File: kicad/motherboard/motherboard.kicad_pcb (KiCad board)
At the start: 4 copper layers, 180.3 x 281.9 mm, 53 parts, among them J1 DB37_Female, J10 DB37_Female, J11 DB37_Female, J12 Barrel_Jack, J13 TSR 1-2433, J2 DB37_Female, J3 DB37_Female, J4 DB37_Female, J5 DB37_Female, J6 DB25_Female, J7 DB37_Female, J8 DB25_Female, J9 DB9_Female, SW1 SW_SPST, U1 SN74ALVC00, U10 SN74ALVC00, U11 SN74ALVC00, U12 SN74ALVC00, U13 SN74ALVC00, U14 SN74ALVC00, U15 SN74ALVC00, U16 SN74ALVC00, U17 SN74ALVC00, U18 SN74ALVC00, U19 SN74ALVC00, U2 SN74ALVC00, U20 SN74ALVC00, U21 SN74ALVC00, U22 SN74ALVC00, U23 SN74ALVC00, U24 SN74ALVC00, U25 SN74ALVC00, U26 SN74ALVC00, U27 SN74ALVC00, U28 SN74ALVC00, U29 SN74ALVC00, U3 SN74ALVC00, U30 SN74ALVC00, U31 SN74ALVC00, U32 SN74ALVC00, U4 SN74ALVC00, U5 SN74ALVC00, U6 SN74ALVC00, U7 SN74ALVC00, U8 SN74ALVC00, U9 SN74ALVC00

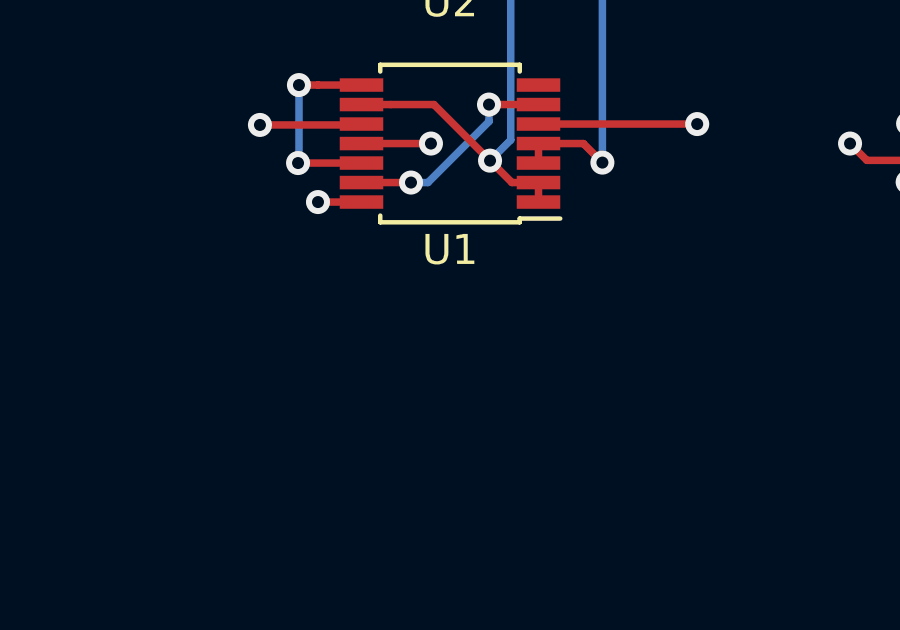
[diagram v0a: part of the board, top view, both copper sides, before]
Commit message: Added clock output enable signal to motherboard debugger. Updated component library.
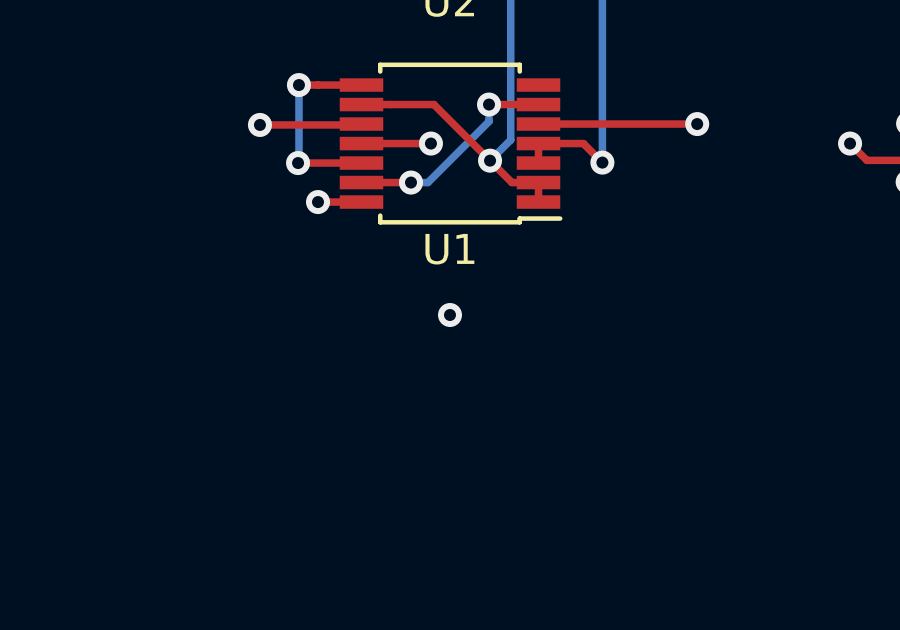
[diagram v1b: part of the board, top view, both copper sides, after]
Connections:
- J11 pad 1: +3V3 -> GND
- J11 pad 20: GND -> clk_oe
- J9 pad 3: Net-(J9-Pad3) -> clk_oe
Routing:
- net clk_oe: track 0.00 -> 297.9 mm, vias 0 -> 1

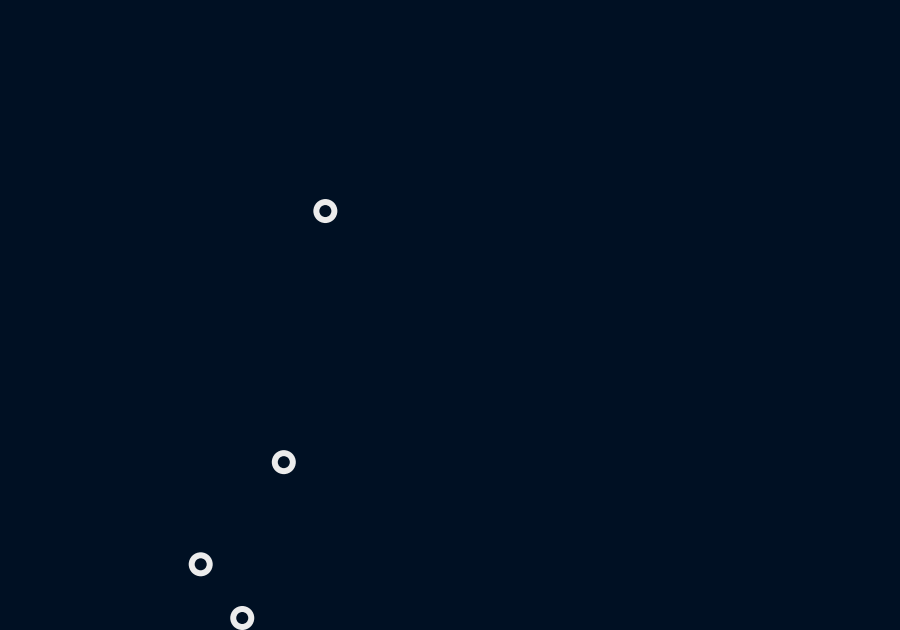
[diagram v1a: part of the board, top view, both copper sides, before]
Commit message: ALU schematic, layout, routing complete. Associated motherboardmod. Also added Load LED to register and program counter boards.
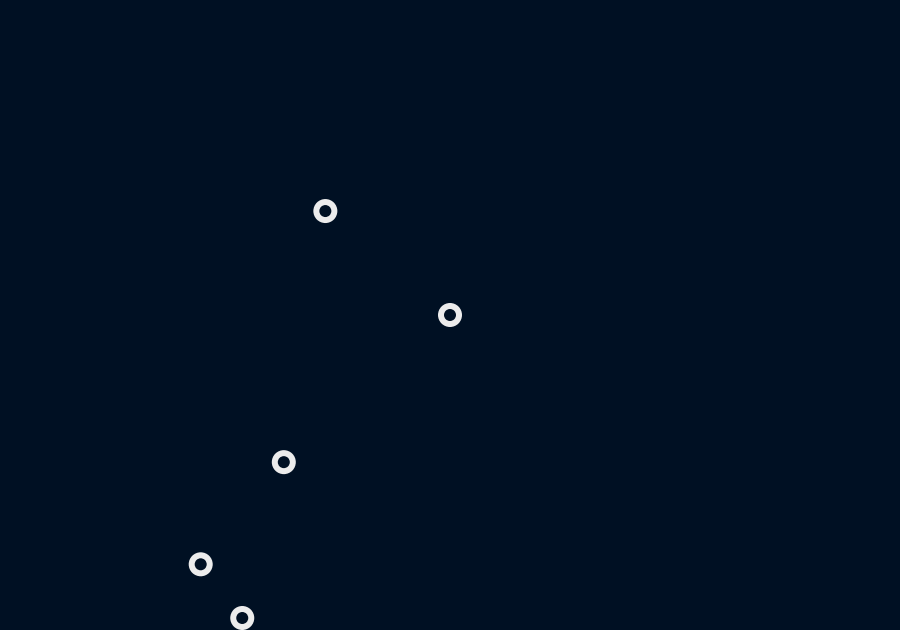
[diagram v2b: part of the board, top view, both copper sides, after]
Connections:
- J6 pad 5: Net-(J6-Pad5) -> inst_15
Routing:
- net inst_15: track 684.6 -> 762.4 mm, vias 20 -> 21
